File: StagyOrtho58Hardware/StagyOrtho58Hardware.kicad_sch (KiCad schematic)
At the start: 83 parts, among them J11 USB_C_Receptacle_USB2.0, SW11 SW_Push, SW12 SW_Push, SW13 SW_Push, SW14 SW_Push, SW15 SW_Push, SW16 SW_Push, SW17 SW_Push, SW18 SW_Push, SW19 SW_Push, SW20 SW_Push, SW21 SW_Push, SW22 SW_Push, SW23 SW_Push, SW24 SW_Push, SW25 SW_Push, SW26 SW_Push, SW27 SW_Push, SW28 SW_Push, SW29 SW_Push, SW30 SW_Push, SW31 SW_Push, SW32 SW_Push, SW33 SW_Push, SW34 SW_Push, SW35 SW_Push, SW36 SW_Push, SW37 SW_Push, SW38 SW_Push, SW39 SW_Push, SW40 SW_Push, U11 Pico, U12 MCP23S17_ML

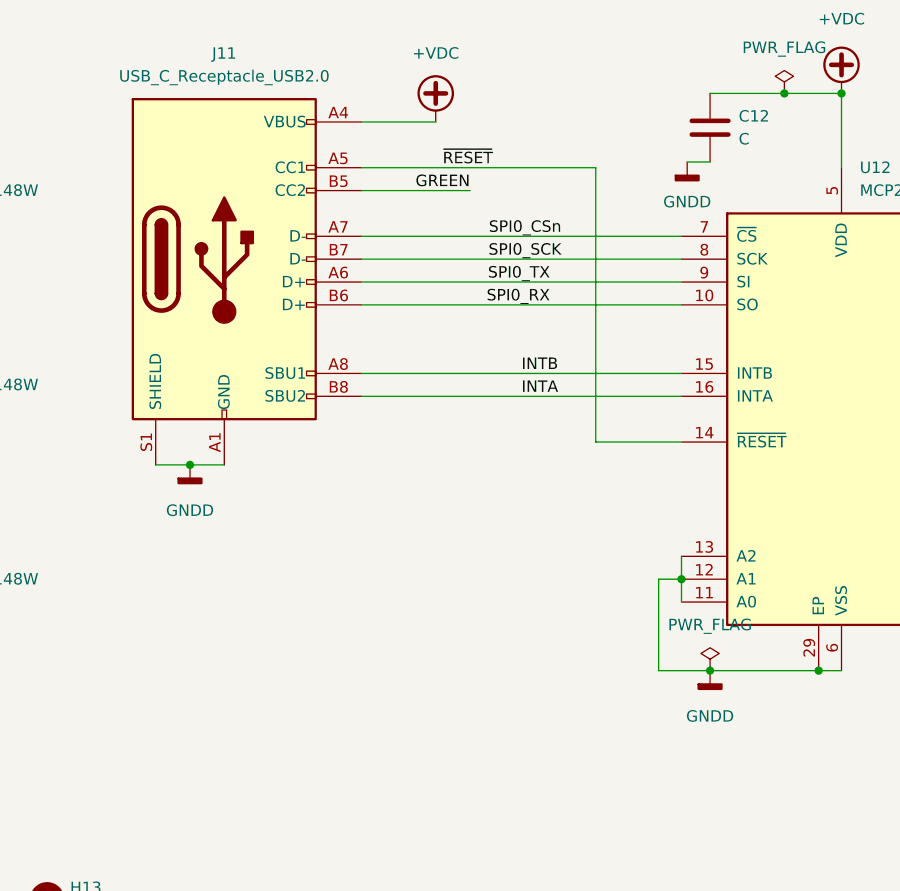
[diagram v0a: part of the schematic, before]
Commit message: Routes rows, columns in switches
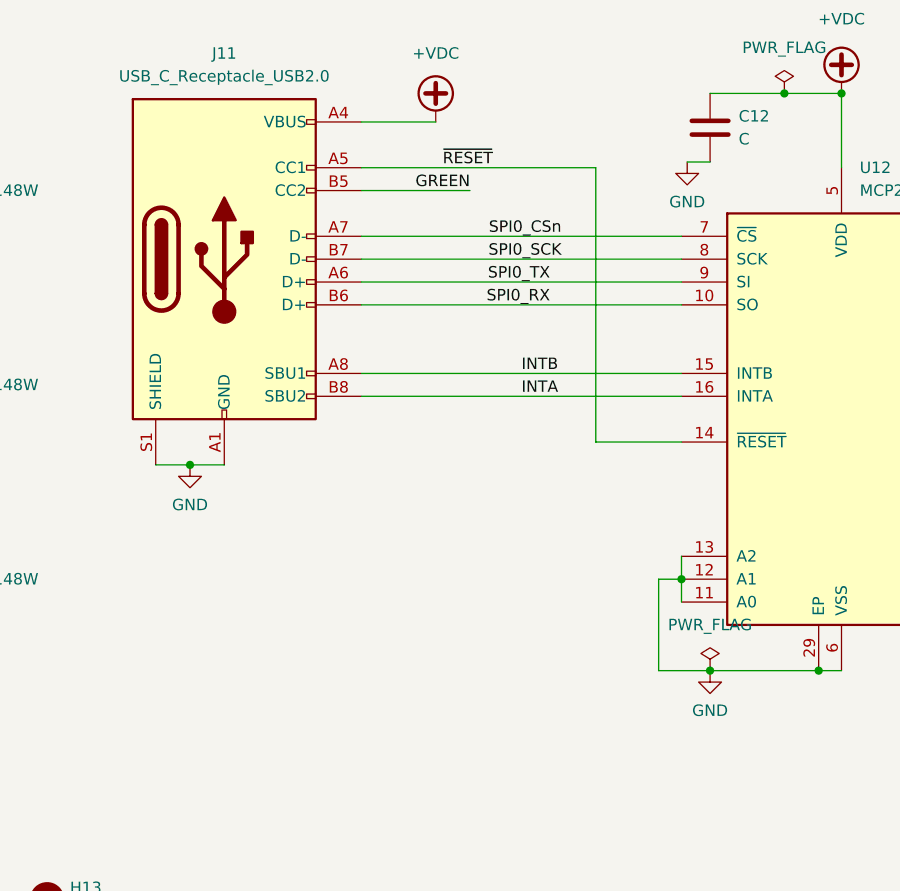
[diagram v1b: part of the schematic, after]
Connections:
- net GNDD is gone; now on net GND: C12.2, J11.A1 (GND), J11.A12 (GND), J11.B1 (GND), J11.B12 (GND), J11.S1 (SHIELD), U12.11 (A0), U12.12 (A1), U12.13 (A2), U12.29 (EP), U12.6 (VSS)

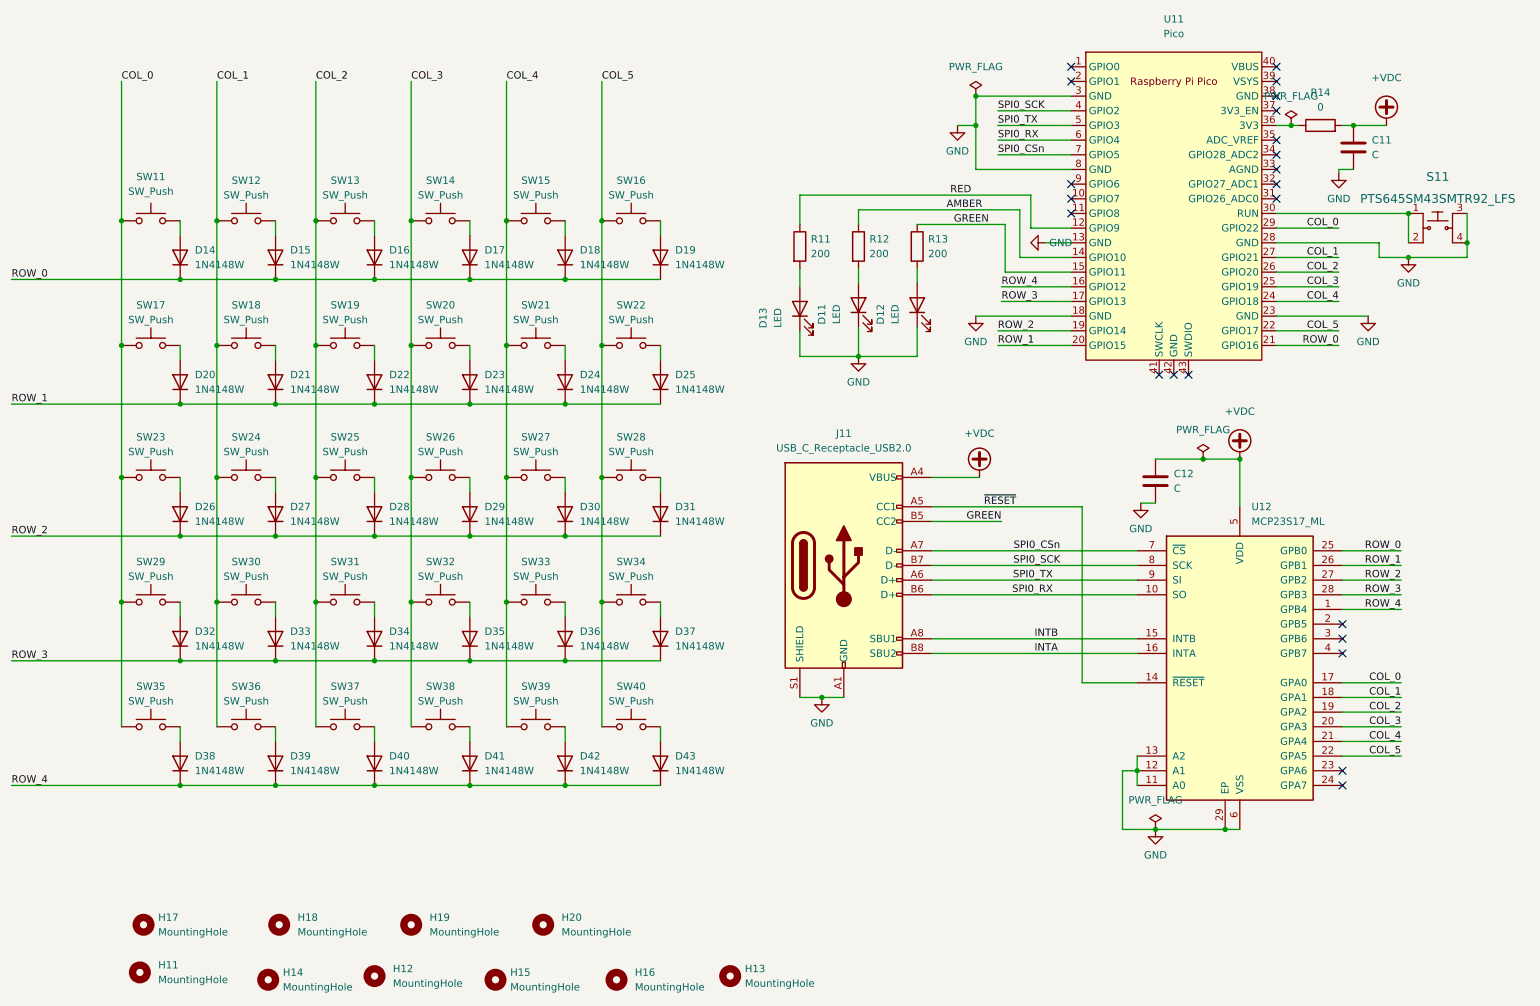
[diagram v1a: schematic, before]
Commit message: Completes routing of the board
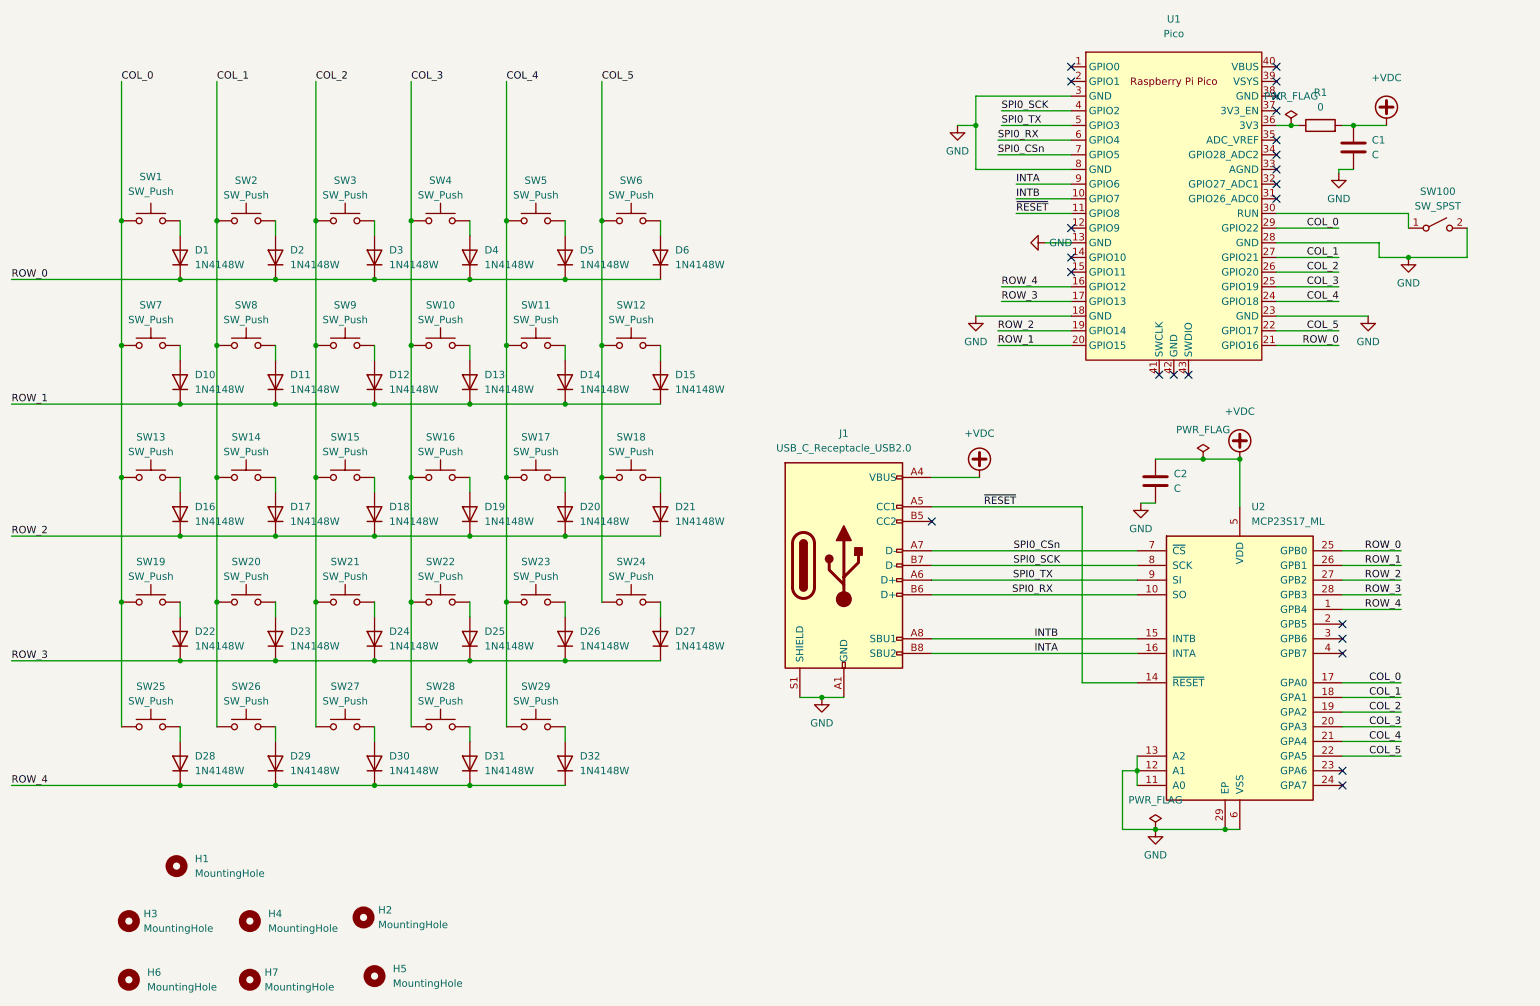
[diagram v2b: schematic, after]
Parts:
- removed D11, D12, D13: LED, LED_SMD:LED_0603_1608Metric_Pad1.05x0.95mm_HandSolder, symbol Device:LED
- removed D43: 1N4148W, Diode_SMD:D_SOD-123, symbol Diode:1N4148W
- removed H17, H18, H19: MountingHole, MountingHole:MountingHole_2.7mm_M2.5, symbol Mechanical:MountingHole
- removed R11, R12, R13: 200, Resistor_SMD:R_0603_1608Metric_Pad0.98x0.95mm_HandSolder, symbol Device:R
- removed S11: PTS645SM43SMTR92_LFS, digikey-footprints:Switch_Tactile_SMD_6x6mm_PTS645, symbol dk_Tactile-Switches:PTS645SM43SMTR92_LFS
- removed SW40: SW_Push, Switch_Keyboard_Kailh:SW_Kailh_Choc_V1V2_1.00u, symbol Switch:SW_Push
- added SW100: SW_SPST, Button_Switch_SMD:SW_SPST_CK_RS282G05A3, symbol Switch:SW_SPST
- U1: renamed from U11; footprint RPi_Pico:RPi_Pico_SMD_TH -> MCU_RaspberryPi_and_Boards:RPi_Pico_SMD_TH
- renumbered C11 to C1, C12 to C2, D14 to D1, D20 to D10, D21 to D11, D22 to D12, D23 to D13, D24 to D14, D25 to D15, D26 to D16, D27 to D17, D28 to D18, D29 to D19, D15 to D2, D30 to D20, D31 to D21, D32 to D22, D33 to D23, D34 to D24, D35 to D25, D36 to D26, D37 to D27, D38 to D28, D39 to D29, D16 to D3, D40 to D30, D41 to D31, D42 to D32, D17 to D4, D18 to D5, D19 to D6, H20 to H1, H13 to H2, H15 to H3, H16 to H4, H12 to H5, H11 to H6, H14 to H7, J11 to J1, R14 to R1, SW11 to SW1, SW20 to SW10, SW21 to SW11, SW22 to SW12, SW23 to SW13, SW24 to SW14, SW25 to SW15, SW26 to SW16, SW27 to SW17, SW28 to SW18, SW29 to SW19, SW12 to SW2, SW30 to SW20, SW31 to SW21, SW32 to SW22, SW33 to SW23, SW34 to SW24, SW35 to SW25, SW36 to SW26, SW37 to SW27, SW38 to SW28, SW39 to SW29, SW13 to SW3, SW14 to SW4, SW15 to SW5, SW16 to SW6, SW17 to SW7, SW18 to SW8, SW19 to SW9, U12 to U2
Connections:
- net GND: now also SW100.2 (B)
- net INTA: now also U1.9 (GPIO6)
- net INTB: now also U1.10 (GPIO7)
- net ~{RESET}: now also U1.11 (GPIO8)
- net at U1.30 (RUN): now also SW100.1 (A)
- net AMBER: no longer names the net of U1.14 (GPIO10)
- net GREEN: no longer names the net of U1.15 (GPIO11)
- net GREEN: no longer J1.B5 (CC2)
- net RED: no longer names the net of U1.12 (GPIO9)
- no-connect marks 22 -> 23
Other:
- moved on the sheet: H1, H2, H3, H4, H6, H7
